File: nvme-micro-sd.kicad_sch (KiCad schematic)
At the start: 32 parts, among them J501 Bus_M.2_1-2199230-6, J502 MicroSD_1140084168, M501 Mech_M2_2280_H2.5mm

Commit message: [#61534] Clean DNP properites
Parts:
- M501: DNP (none) -> DNP; now not fitted
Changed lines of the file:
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@@
   )
   (symbol (lib_id "antmicroModules:Mech_M2_2280_H2.5mm") (at 234.95 121.92 180) (unit 1)
-    (in_bom no) (on_board yes) (dnp no) (fields_autoplaced)
-    (property "Reference" "M501" (at 229.87 107.95 0)
+    (in_bom no) (on_board yes) (dnp yes) (fields_autoplaced)
+    (property "Reference" "M501" (at 229.87 124.46 0)
       (effects (font (size 1.27 1.27)))
     )
-    (property "Value" "Mech_M2_2280_H2.5mm" (at 229.87 110.49 0)
+    (property "Value" "Mech_M2_2280_H2.5mm" (at 229.87 127 0)
       (effects (font (size 1.27 1.27) (thickness 0.15)))
     )
@@
       (effects (font (size 1.27 1.27) (thickness 0.15)) (justify left bottom) hide)
     )
+    (property "DNP" "DNP" (at 229.87 129.54 0)
+      (effects (font (size 1.27 1.27)))
+    )
     (instances

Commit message: [#63565] Synchronize components with library, bump revision to 1.0.4
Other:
- company: Antmicro -> Antmicro Ltd
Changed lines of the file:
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@@
   (title_block
     (title "CM4 Baseboard")
-    (date "2024-06-19")
-    (rev "1.0.3")
-    (company "Antmicro")
+    (date "2024-08-02")
+    (rev "1.0.5")
+    (company "Antmicro Ltd")
     (comment 1 "www.antmicro.com")
   )

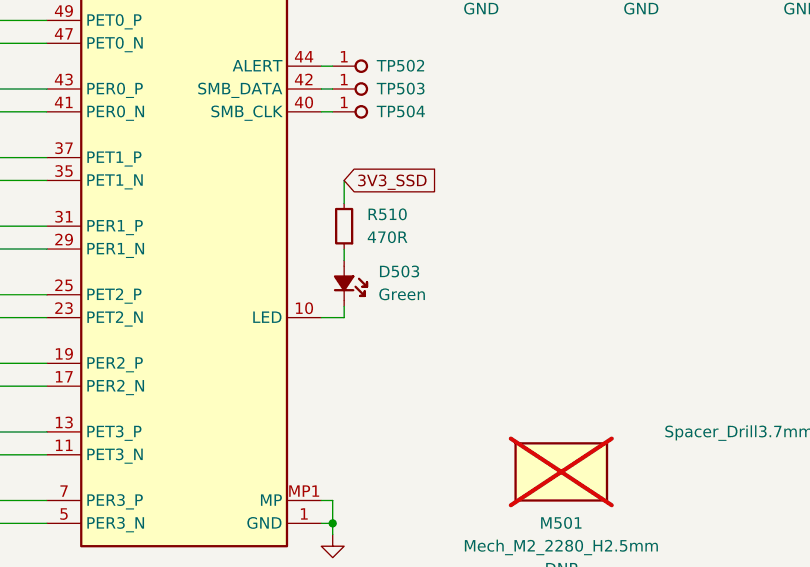
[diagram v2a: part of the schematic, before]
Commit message: [#65638] Fix green LEDs, bump revision to 1.0.5
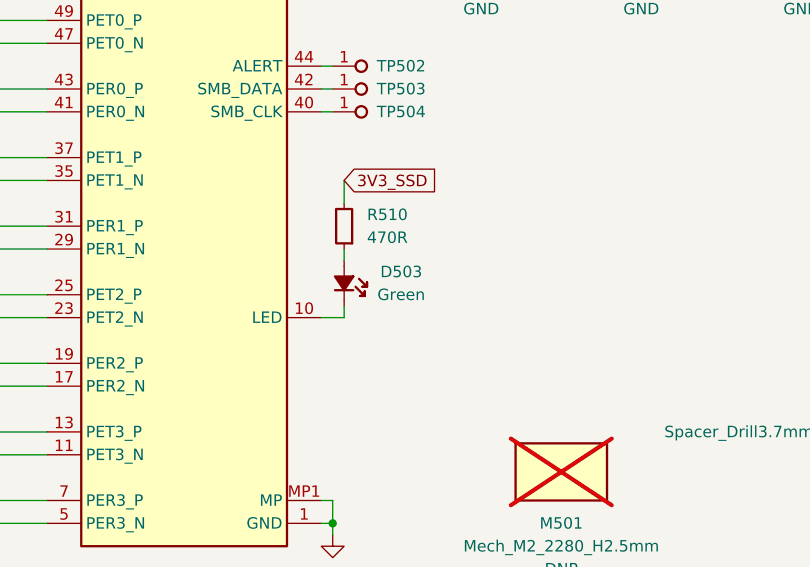
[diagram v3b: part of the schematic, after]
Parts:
- removed D503: LED_G_0603_598-8D80-107F, antmicro-footprints:LED_0603_1608Metric_G, symbol antmicroLEDIndicationDiscrete:LED_G_0603_598-8D80-107F
- added D503: LED_G_0603_KP-1608CGCK, antmicro-footprints:LED_0603_1608Metric_G, symbol antmicroLEDIndicationDiscrete:LED_G_0603_KP-1608CGCK
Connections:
- net at R510.1: now also D503.2 (A)
- net at J501.10 (LED): now also D503.1 (C)
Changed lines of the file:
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@@
   (title_block
     (title "CM4 Baseboard")
-    (date "2024-08-02")
+    (date "2024-09-12")
     (rev "1.0.5")
     (company "Antmicro Ltd")
@@
     )
   )
+  (symbol (lib_id "antmicroLEDIndicationDiscrete:LED_G_0603_KP-1608CGCK") (at 205.74 100.33 270) (mirror x) (unit 1)
+    (in_bom yes) (on_board yes) (dnp no)
+    (property "Reference" "D503" (at 212.09 96.52 90)
+      (effects (font (size 1.27 1.27) (thickness 0.15)))
+    )
+    (property "Value" "LED_G_0603_KP-1608CGCK" (at 198.12 77.47 0)
+      (effects (font (size 1.27 1.27) (thickness 0.15)) (justify left bottom) hide)
+    )
+    (property "Footprint" "antmicro-footprints:LED_0603_1608Metric_G" (at 195.58 77.47 0)
+      (effects (font (size 1.27 1.27) (thickness 0.15)) (justify left bottom) hide)
+    )
+    (property "Datasheet" "http://www.kingbright.com/attachments/file/psearch//000/00/00/KP-1608CGCK(Ver.23B).pdf" (at 193.04 77.47 0)
+      (effects (font (size 1.27 1.27) (thickness 0.15)) (justify left bottom) hide)
+    )
+    (property "MPN" "KP-1608CGCK" (at 190.5 77.47 0)
+      (effects (font (size 1.27 1.27) (thickness 0.15)) (justify left bottom) hide)
+    )
+    (property "Manufacturer" "Kingbright" (at 187.96 77.47 0)
+      (effects (font (size 1.27 1.27) (thickness 0.15)) (justify left bottom) hide)
+    )
+    (property "Color" "Green" (at 212.09 99.06 90)
+      (effects (font (size 1.27 1.27)))
+    )
+    (property "Author" "Antmicro" (at 185.42 77.47 0)
+      (effects (font (size 1.27 1.27) (thickness 0.15)) (justify left bottom) hide)
+    )
+    (property "License" "Apache-2.0" (at 182.88 77.47 0)
+      (effects (font (size 1.27 1.27) (thickness 0.15)) (justify left bottom) hide)
+    )
+    (pin "2")
+    (pin "1")
+    (instances
+      (project "cm4-baseboard"
+        (path "/60b842dc-0853-4a25-99ac-5784ddf94d0d/00000000-0000-0000-0000-00005fea1b94"
+          (reference "D503") (unit 1)
+        )
+      )
+    )
+  )
   (symbol (lib_id "antmicroMechanicalParts:Spacer_Drill3.7mm_H2.5mm_9774025151R") (at 265.43 119.38 180) (unit 1)
     (in_bom yes) (on_board yes) (dnp no) (fields_autoplaced)
@@
         )
       )
-    )
-  )
-  (symbol (lib_id "antmicroLEDIndicationDiscrete:LED_G_0603_598-8D80-107F") (at 205.74 100.33 270) (mirror x) (unit 1)
-    (in_bom yes) (on_board yes) (dnp no) (fields_autoplaced)
-    (property "Reference" "D503" (at 209.55 96.52 90)
-      (effects (font (size 1.27 1.27) (thickness 0.15)) (justify left))
-    )
-    (property "Value" "LED_G_0603_598-8D80-107F" (at 198.12 77.47 0)
-      (effects (font (size 1.27 1.27) (thickness 0.15)) (justify left bottom) hide)
-    )
-    (property "Footprint" "antmicro-footprints:LED_0603_1608Metric_G" (at 195.58 77.47 0)
-      (effects (font (size 1.27 1.27) (thickness 0.15)) (justify left bottom) hide)
-    )
-    (property "Datasheet" "https://www.dialight.com/wp-content/uploads/2021/07/DIA_Selector_Guide_SMD_042321.pdf" (at 193.04 77.47 0)
-      (effects (font (size 1.27 1.27) (thickness 0.15)) (justify left bottom) hide)
-    )
-    (property "MPN" "598-8D80-107F" (at 190.5 77.47 0)
-      (effects (font (size 1.27 1.27) (thickness 0.15)) (justify left bottom) hide)
-    )
-    (property "Manufacturer" "Dialight" (at 187.96 77.47 0)
-      (effects (font (size 1.27 1.27) (thickness 0.15)) (justify left bottom) hide)
-    )
-    (property "Author" "Antmicro" (at 185.42 77.47 0)
-      (effects (font (size 1.27 1.27) (thickness 0.15)) (justify left bottom) hide)
-    )
-    (property "License" "Apache-2.0" (at 182.88 77.47 0)
-      (effects (font (size 1.27 1.27) (thickness 0.15)) (justify left bottom) hide)
-    )
-    (property "Color" "Green" (at 209.55 99.06 90)
-      (effects (font (size 1.27 1.27)) (justify left))
-    )
-    (pin "1")
-    (pin "2")
-    (instances
-      (project "cm4-baseboard"
-        (path "/60b842dc-0853-4a25-99ac-5784ddf94d0d/00000000-0000-0000-0000-00005fea1b94"
-          (reference "D503") (unit 1)
-        )
-      )
